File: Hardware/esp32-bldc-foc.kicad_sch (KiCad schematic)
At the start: 59 parts, among them J1 ENCODER, J2 I2C2, J3 VDRIVE, J4 MOTOR, P1 PCB_Pin_Breakout, P10 PCB_Pin_Breakout, P11 PCB_Pin_Breakout, P12 PCB_Pin_Breakout, P13 PCB_Pin_Breakout, P14 PCB_Pin_Breakout, P15 PCB_Pin_Breakout, P16 PCB_Pin_Breakout, P17 PCB_Pin_Breakout, P18 PCB_Pin_Breakout, P19 PCB_Pin_Breakout, P2 PCB_Pin_Breakout, P20 PCB_Pin_Breakout, P21 PCB_Pin_Breakout, P22 PCB_Patch, P23 PCB_Patch, P24 PCB_Patch, P25 PCB_Patch, P26 PCB_Patch, P27 PCB_Patch, P28 PCB_Patch, P29 PCB_Patch, P3 PCB_Pin_Breakout, P30 PCB_Patch, P31 PCB_Patch, P32 PCB_Patch, P33 PCB_Patch, P34 PCB_Patch, P35 PCB_Patch, P36 PCB_Patch, P37 PCB_Patch, P38 PCB_Patch, P39 PCB_Patch, P4 PCB_Pin_Breakout, P40 PCB_Patch, P5 PCB_Pin_Breakout, P6 PCB_Pin_Breakout, P7 PCB_Pin_Breakout, P8 PCB_Pin_Breakout, P9 PCB_Pin_Breakout, U1 ESP32-S3-WROOM-1, U3 SRV05-4, U6 EG2133

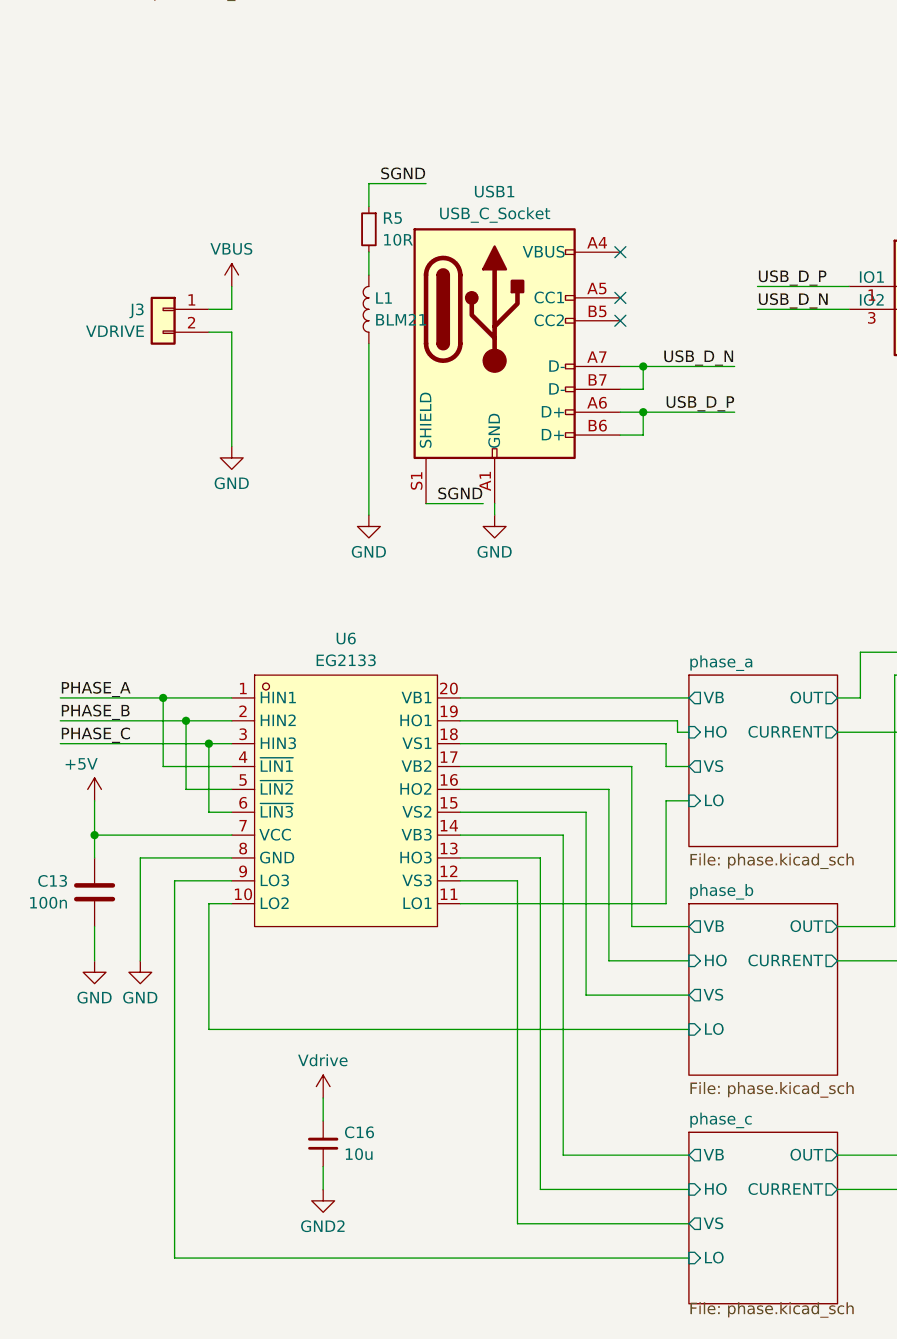
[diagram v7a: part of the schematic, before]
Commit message: Second cut of circuit board
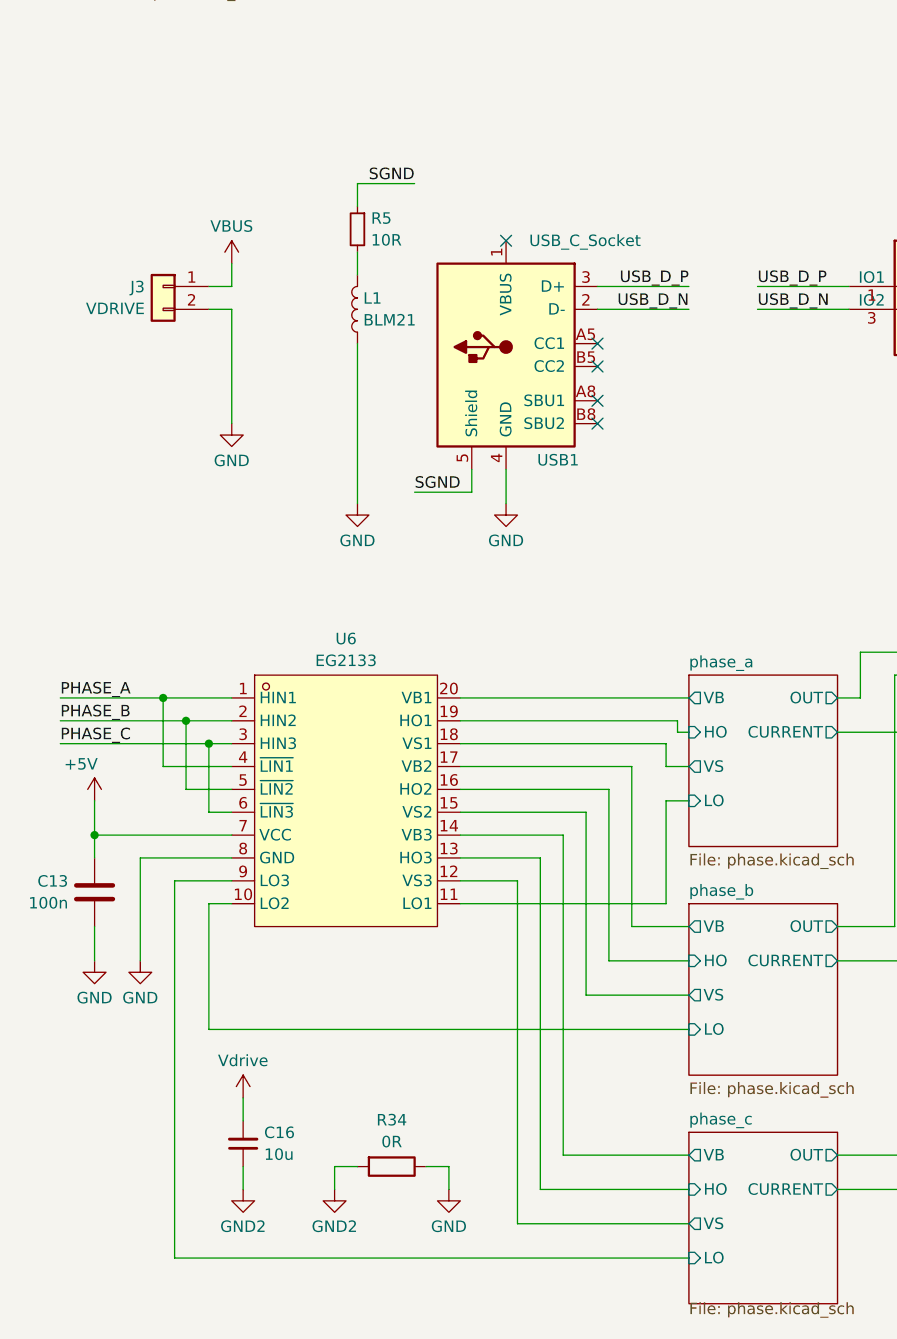
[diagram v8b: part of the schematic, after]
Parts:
- added R34: 0R, Resistor_SMD:R_0603_1608Metric, symbol Device:R
- C13, C2, C3: footprint (none) -> Capacitor_SMD:C_0603_1608Metric
- J1: footprint (none) -> Connector_PinSocket_2.54mm:PinSocket_1x06_P2.54mm_Vertical
- R1, R3, R5: footprint (none) -> Resistor_SMD:R_0603_1608Metric
- USB1: footprint (none) -> afork-kicad-parts:Tinker-USB_C; symbol afork-kicad-parts:USB_C_Receptacle_USB2.0_14P -> afork-kicad-parts:Tinker-USB_C; LCSC (none) -> C2765186
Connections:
- net GND: now also USB1.4 (GND), R34.1; no longer USB1.A1 (GND), USB1.A12 (GND), USB1.B1 (GND), USB1.B12 (GND)
- net GND2: now also R34.2
- net SGND: now also USB1.5 (Shield); no longer USB1.S1 (SHIELD)
- net USB_D_N: now also USB1.2 (D-); no longer USB1.A7 (D-), USB1.B7 (D-)
- net USB_D_P: now also USB1.3 (D+); no longer USB1.A6 (D+), USB1.B6 (D+)
- no-connect marks 4 -> 6
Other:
- moved on the sheet: C16, J3, L1, R5
